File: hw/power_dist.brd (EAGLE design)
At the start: 80 x 50 mm, 97 parts, among them J1 JST-ZH6SMT_VERT, J2 JST-PH4SMT_VERT, J3 JST-PH5VERT, P1 XT30P, P2 XT30P, P3 XT30P, P4 XT30P, P5 XT30P, P6 XT30P, P7 XT90PW-M, Q1 PSMN4R8-100BSEJ, Q2 PSMN4R8-100BSEJ, Q3 PSMN4R8-100BSEJ, U1 MAX15062AATA+T, U2 STM32G474CEU6, U3 TPS2490DGSR, U4 TCAN334G, U5 LT1787HVIMS8PBF, U6 STLM20DD9FUDFN-4L_STM-L

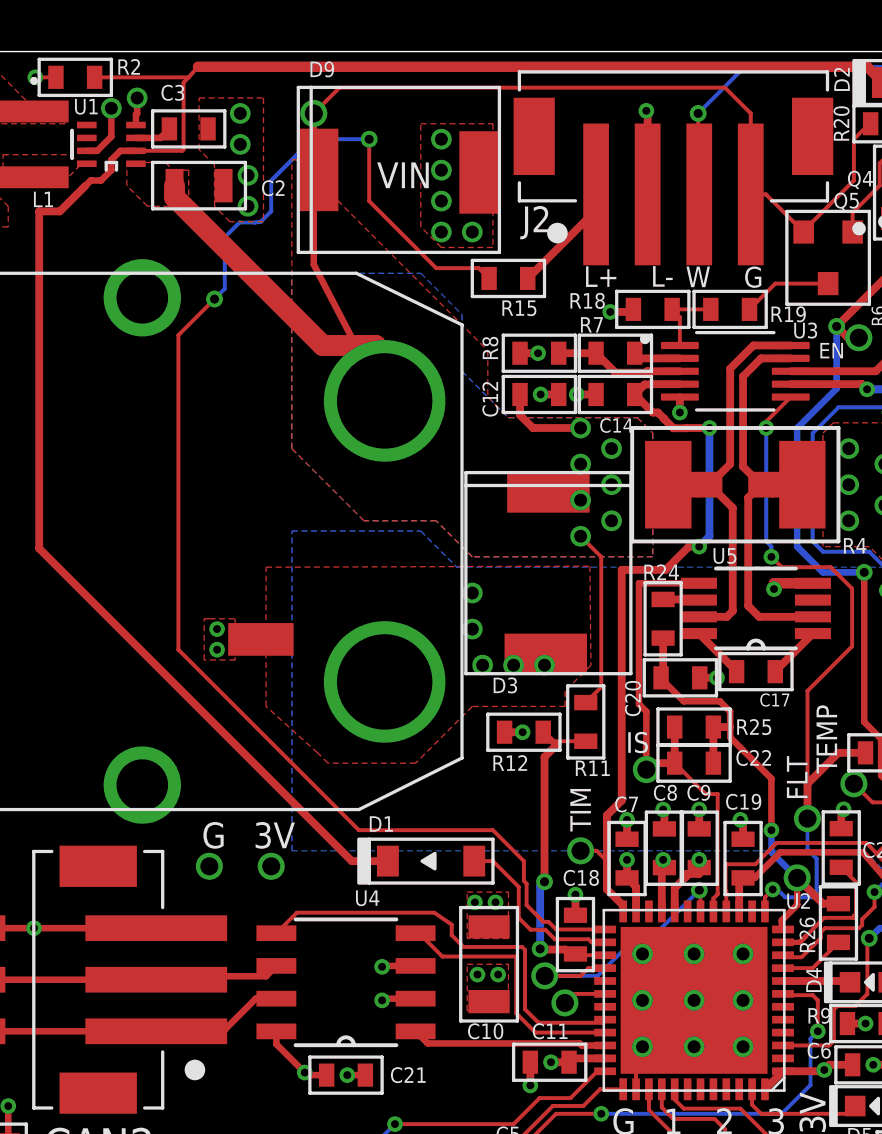
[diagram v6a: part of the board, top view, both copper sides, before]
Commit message: Minor position tweaks after gerber viewing
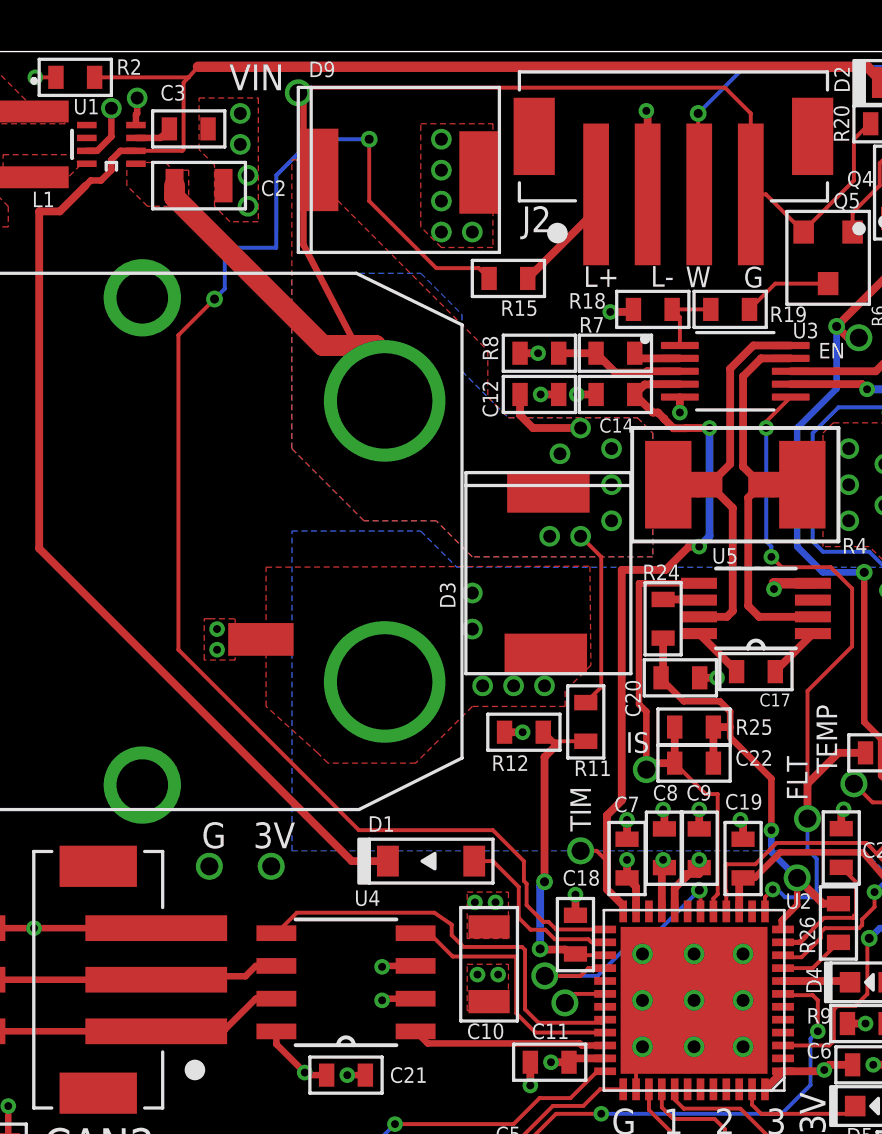
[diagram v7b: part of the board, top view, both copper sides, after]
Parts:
- moved DB_VIN 1.00 mm to (20.1, 48.4)
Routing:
- net +24V: track 63.9 -> 65.1 mm
- net PWR_LED: track 54.9 -> 55.6 mm
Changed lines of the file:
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@@
 <text x="16.3" y="19.1" size="1" layer="21">G</text>
 <text x="18.3" y="19.1" size="1" layer="21">3V</text>
-<text x="23.1" y="44.7" size="1" layer="21">VIN</text>
+<text x="19.5" y="49.5" size="1" layer="21" rot="R180">VIN</text>
 <text x="67.3" y="46.9" size="1" layer="21">VSW</text>
 <text x="39.8" y="20.95" size="0.8" layer="25" font="vector" ratio="10" rot="R90">FLT</text>
@@
 <element name="D3" library="power_dist" package="DIODE_DO-214AB" value="SMBJ51CA-E3/52214AB" x="29.75" y="29.77" smashed="yes" rot="R270">
 <attribute name="MPN" value="SMC5K51A-M3/I" x="29.75" y="29.77" size="1.778" layer="27" rot="R270" display="off"/>
-<attribute name="NAME" x="27.5534" y="25.115" size="0.6" layer="25" ratio="10" rot="SR0"/>
+<attribute name="NAME" x="26.145" y="28.3934" size="0.6" layer="25" ratio="10" rot="SR90"/>
 <attribute name="POPULATE" value="1" x="29.75" y="29.77" size="1.778" layer="27" rot="R270" display="off"/>
 </element>
@@
 <attribute name="POPULATE" value="0" x="16.2" y="18.8" size="1.778" layer="27" display="off"/>
 </element>
-<element name="DB_VIN" library="precharge" package="24AWG_PAD" value="PAD24AWG_PAD" x="20.65" y="47.6" smashed="yes">
-<attribute name="POPULATE" value="0" x="20.65" y="47.6" size="1.778" layer="27" display="off"/>
+<element name="DB_VIN" library="precharge" package="24AWG_PAD" value="PAD24AWG_PAD" x="20.05" y="48.4" smashed="yes">
+<attribute name="POPULATE" value="0" x="20.05" y="48.4" size="1.778" layer="27" display="off"/>
 </element>
 <element name="DB_VSW" library="precharge" package="24AWG_PAD" value="PAD24AWG_PAD" x="68" y="46" smashed="yes">
@@
 <vertex x="16.2" y="46.2"/>
 <vertex x="16.2" y="48.2"/>
-<vertex x="18.7" y="48.2"/>
-<vertex x="18.7" y="43.4"/>
+<vertex x="18.5" y="48.2"/>
+<vertex x="18.5" y="43.4"/>
 <vertex x="17.4" y="43.4"/>
 </polygon>
@@
 <wire x1="29.25" y1="11.95" x2="28.5" y2="12.7" width="0.1524" layer="1"/>
 <wire x1="28.5" y1="12.7" x2="28.5" y2="14.9" width="0.1524" layer="1"/>
-<wire x1="25.6377875" y1="14.9" x2="24.7327875" y2="15.805" width="0.1524" layer="1"/>
-<wire x1="24.7327875" y1="15.805" x2="24.6" y2="15.805" width="0.1524" layer="1"/>
-<wire x1="28.5" y1="14.9" x2="25.6377875" y2="14.9" width="0.1524" layer="1"/>
+<wire x1="26.0377875" y1="14.9" x2="25.1327875" y2="15.805" width="0.1524" layer="1"/>
+<wire x1="25.1327875" y1="15.805" x2="24.6" y2="15.805" width="0.1524" layer="1"/>
+<wire x1="28.5" y1="14.9" x2="26.0377875" y2="14.9" width="0.1524" layer="1"/>
 </signal>
 <signal name="CAN_TX">
@@
 <wire x1="5.94" y1="14" x2="14.54" y2="14" width="0.254" layer="1"/>
 <wire x1="14.54" y1="14" x2="14.60686875" y2="14.135" width="0.254" layer="1"/>
-<wire x1="18.8" y1="14.135" x2="14.60686875" y2="14.135" width="0.254" layer="1"/>
-<wire x1="18.8" y1="14.135" x2="19.2" y2="14.535" width="0.254" layer="1"/>
+<wire x1="18" y1="14.135" x2="14.60686875" y2="14.135" width="0.254" layer="1"/>
+<wire x1="18.4" y1="14.535" x2="18" y2="14.135" width="0.254" layer="1"/>
+<wire x1="18.4" y1="14.535" x2="19.2" y2="14.535" width="0.254" layer="1"/>
 </signal>
 <signal name="CAN_SHDN">
@@
 <via x="16.8" y="40.4" extent="1-16" drill="0.35"/>
 <wire x1="16.8" y1="40.4" x2="17.2" y2="40.8" width="0.1524" layer="16"/>
-<wire x1="17.2" y1="40.8" x2="17.2" y2="42.8" width="0.1524" layer="16"/>
-<wire x1="17.769" y1="43.369" x2="17.2" y2="42.8" width="0.1524" layer="16"/>
-<wire x1="17.769" y1="43.369" x2="18.361375" y2="43.369" width="0.1524" layer="16"/>
-<wire x1="18.361375" y1="43.369" x2="18.6" y2="43.4" width="0.1524" layer="16"/>
-<wire x1="18.6" y1="43.4" x2="19" y2="43.8" width="0.1524" layer="16"/>
-<wire x1="19" y1="43.8" x2="19" y2="45" width="0.1524" layer="16"/>
-<wire x1="19" y1="45" x2="20.6" y2="46.6" width="0.1524" layer="16"/>
+<wire x1="17.2" y1="40.8" x2="17.2" y2="42.39214375" width="0.1524" layer="16"/>
+<wire x1="17.2" y1="42.39214375" x2="19.19401875" y2="42.3897625" width="0.1524" layer="16"/>
+<wire x1="19.19401875" y1="42.3897625" x2="19.200459375" y2="45.200459375" width="0.1524" layer="16"/>
+<wire x1="19.200459375" y1="45.200459375" x2="20.6" y2="46.6" width="0.1524" layer="16"/>
 <wire x1="22.8" y1="46.6" x2="20.6" y2="46.6" width="0.1524" layer="16"/>
 <via x="22.8" y="46.6" extent="1-16" drill="0.35"/>
@@
 <via x="31" y="35.4" extent="1-16" drill="0.5"/>
 <via x="32.2" y="34.6" extent="1-16" drill="0.5"/>
-<via x="31" y="34" extent="1-16" drill="0.5"/>
+<via x="30.2" y="34.4" extent="1-16" drill="0.5"/>
 <via x="32.2" y="33.2" extent="1-16" drill="0.5"/>
-<via x="31" y="32.6" extent="1-16" drill="0.5"/>
+<via x="29.8" y="31.2" extent="1-16" drill="0.5"/>
 <via x="32.2" y="31.8" extent="1-16" drill="0.5"/>
 <via x="31" y="31.2" extent="1-16" drill="0.5"/>
@@
 <wire x1="28.65" y1="36.7" x2="28.65" y2="35.9" width="0.3048" layer="1"/>
 <wire x1="29.15" y1="35.4" x2="31" y2="35.4" width="0.3048" layer="1"/>
-<wire x1="20.65" y1="47.6" x2="20.65" y2="41.7384625" width="0.254" layer="1"/>
-<wire x1="20.65" y1="41.7384625" x2="23.4" y2="36.45" width="0.254" layer="1"/>
+<wire x1="20.05" y1="48.4" x2="20.25" y2="48.2" width="0.254" layer="1"/>
+<wire x1="20.25" y1="48.2" x2="20.25" y2="42.50769375" width="0.254" layer="1"/>
+<wire x1="20.25" y1="42.50769375" x2="23.4" y2="36.45" width="0.254" layer="1"/>
 <contactref element="D9" pad="P$1"/>
 <contactref element="Q5" pad="P$2"/>
@@
 <wire x1="37.6" y1="44.46" x2="37.6" y2="47.6" width="0.1524" layer="1"/>
 <wire x1="37.6" y1="47.6" x2="36.6" y2="48.6" width="0.1524" layer="1"/>
-<wire x1="36.6" y1="48.6" x2="21.65" y2="48.6" width="0.1524" layer="1"/>
-<wire x1="21.65" y1="48.6" x2="20.65" y2="47.6" width="0.1524" layer="1"/>
+<wire x1="36.6" y1="48.6" x2="20.25" y2="48.6" width="0.1524" layer="1"/>
+<wire x1="20.25" y1="48.6" x2="20.05" y2="48.4" width="0.1524" layer="1"/>
 <wire x1="37.6" y1="44.46" x2="38.19" y2="44.46" width="0.1524" layer="1"/>
 <wire x1="38.19" y1="44.46" x2="39.65" y2="43" width="0.1524" layer="1"/>
@@
 <vertex x="19.8" y="19"/>
 </polygon>
-<via x="29.6" y="26.2" extent="1-16" drill="0.5"/>
-<via x="28.4" y="26.2" extent="1-16" drill="0.5"/>
-<via x="27.2" y="26.2" extent="1-16" drill="0.5"/>
+<via x="29.6" y="25.4" extent="1-16" drill="0.5"/>
+<via x="28.4" y="25.4" extent="1-16" drill="0.5"/>
+<via x="27.2" y="25.4" extent="1-16" drill="0.5"/>
 <via x="26.8" y="27.6" extent="1-16" drill="0.5"/>
 <via x="26.8" y="29" extent="1-16" drill="0.5"/>

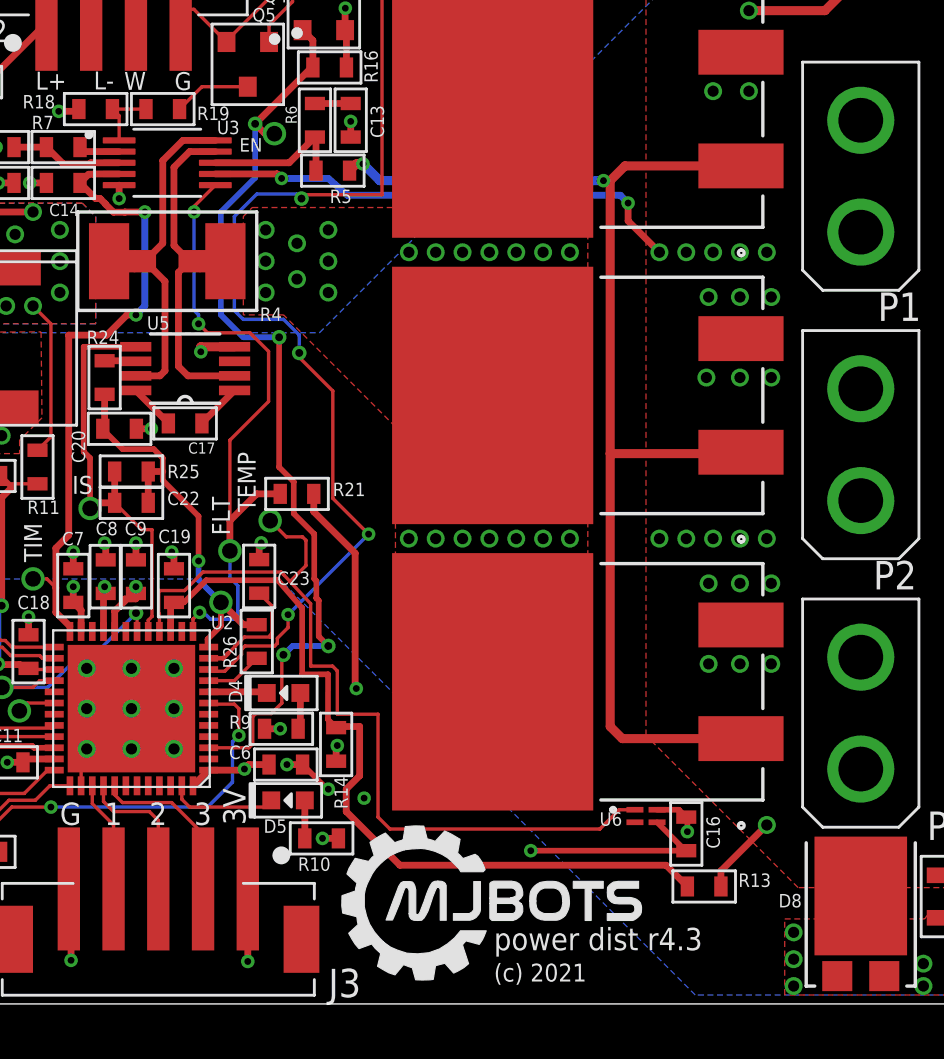
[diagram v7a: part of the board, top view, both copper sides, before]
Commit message: Add part numbers, rev to 4.3b
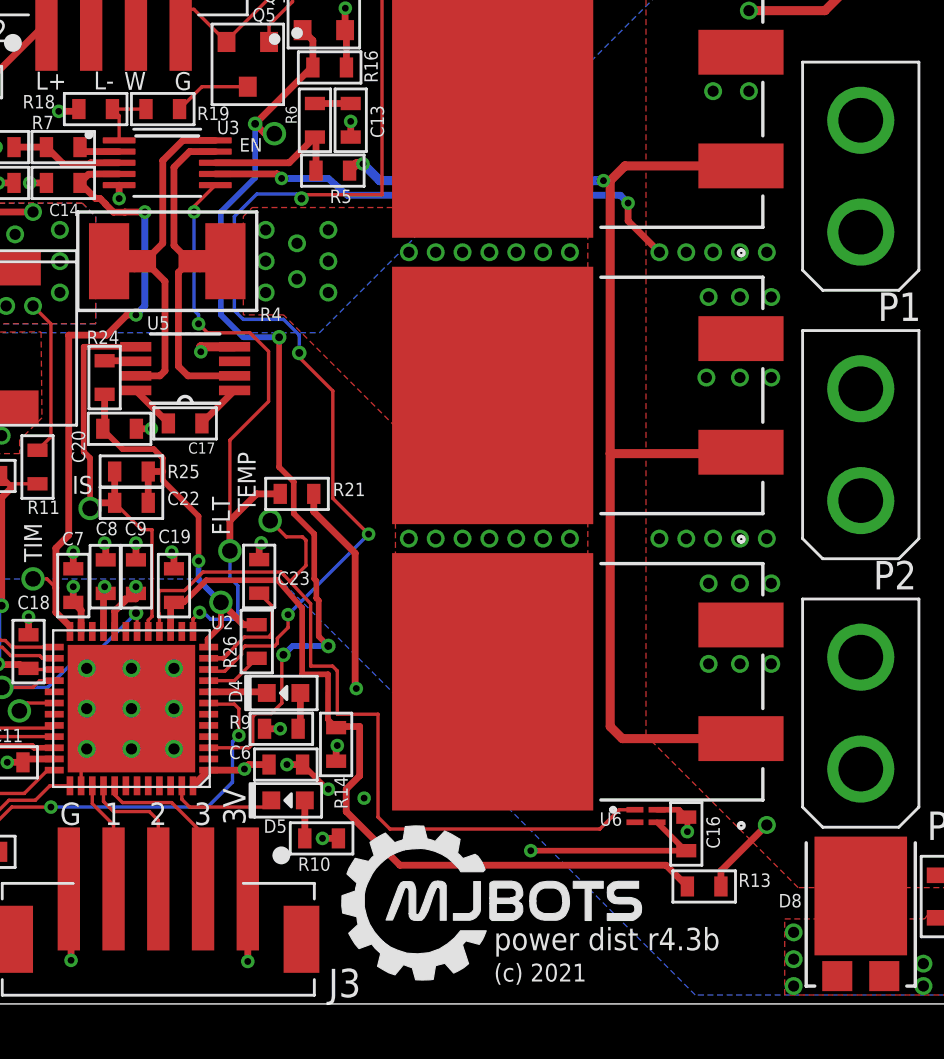
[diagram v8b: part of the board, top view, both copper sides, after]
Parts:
- C10, C4: value 10uF 50V -> 10uF
- R18: value 100k 1% -> 140k 1%
- R22: value 200k 1% -> 100k
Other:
- board text added: "power dist r4.3b"
- board text removed: "power dist r4.3"
